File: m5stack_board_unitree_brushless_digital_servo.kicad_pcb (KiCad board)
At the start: 2 copper layers, 50 x 35 mm, 28 parts, among them J1 XT30UPB-M, J2 ZX-HY2.0-4PZZ, J3 B3B-PH-K-S(LF)(SN), J4 B3B-PH-K-S(LF)(SN), J5 B3B-PH-K-S(LF)(SN), J6 B3B-PH-K-S(LF)(SN), J7 B3B-PH-K-S(LF)(SN), U1 74LVC1G14, U2 AP7333-33SAG, U3 74LVC1G126, U4 74LVC1G125

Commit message: Use the Basic part XC6206P332MR for U2
U2 was the AP7333-33SAG carried over from the DYNAMIXEL board: an Extended
part with the lowest stock in the BOM (about 16k). The Torex XC6206P332MR-G
(C5446) is a Basic part (no feeder loading fee in Economic PCBA, about 420k
in stock) and covers the few mA the logic draws (200 mA, 6 V input, stable
with the 1 uF C2 and C3).

Its pins differ (1 GND, 2 output, 3 input), so:
- the schematic uses the KiCad XC6206PxxxMR symbol (same pin positions);
- on the board, C2 + feeds pin 3, pin 1 gets a GND via above it, the +5V
  line above U2 moves up 0.45 mm to keep that via clear of its pour
  clearance, and C2 - now joins C3 -;
- the CPL keeps +180 (same land pattern orientation as before).

DRC, ERC and the board checks are clean; the README images are updated.

Co-Authored-By: Claude Opus 5.5 <noreply@anthropic.com>
Claude-Session: https://claude.ai/code/session_01WJ1YBGdXpG8xhBv94Snq4Y
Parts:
- U2: value AP7333-33SAG -> XC6206P332MR
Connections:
- U2 pad 1: +5V -> GND
- U2 pad 3: GND -> +5V
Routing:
- net +5V: track 18.6 -> 19.6 mm
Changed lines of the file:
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@@
 			)
 		)
-		(property "Value" "AP7333-33SAG"
+		(property "Value" "XC6206P332MR"
 			(at 0 2.4 0)
 			(layer "F.Fab")
@@
 			)
 		)
-		(property "Datasheet" "https://www.diodes.com/assets/Datasheets/AP7384.pdf"
+		(property "Datasheet" "https://www.torexsemi.com/file/xc6206/XC6206.pdf"
 			(at 0 0 0)
 			(layer "F.Fab")
@@
 			)
 		)
-		(property "LCSC" "C150746"
+		(property "LCSC" "C5446"
 			(at 0 0 0)
 			(layer "F.Fab")
@@
 			(layers "F.Cu" "F.Mask" "F.Paste")
 			(roundrect_rratio 0.25)
-			(net 5 "+5V")
+			(net 2 "GND")
 		)
 		(pad "2" smd roundrect
@@
 			(layers "F.Cu" "F.Mask" "F.Paste")
 			(roundrect_rratio 0.25)
-			(net 2 "GND")
+			(net 5 "+5V")
 		)
 		(embedded_fonts no)
@@
 	)
 	(segment
+		(start 152.963 121.3)
+		(end 152.963 120.55)
+		(width 0.4)
+		(layer "F.Cu")
+		(net 2)
+	)
+	(segment
 		(start 158.3 121.3875)
 		(end 158.3 120.35)
@@
 	)
 	(segment
-		(start 156.7 123.1125)
-		(end 154.84 121.45)
+		(start 156.7 123.112)
+		(end 158.3 121.512)
 		(width 0.4)
 		(layer "F.Cu")
@@
 	)
 	(segment
-		(start 154.8375 122.25)
-		(end 154.84 121.45)
-		(width 0.4)
-		(layer "F.Cu")
-		(net 2)
-	)
-	(segment
 		(start 146 123.1)
 		(end 147.35 123.1)
@@
 	)
 	(via
-		(at 154.84 121.45)
+		(at 152.963 120.55)
 		(size 0.605)
 		(drill 0.3)
@@
 	)
 	(segment
-		(start 152.96 119.75)
-		(end 156.2 119.75)
+		(start 155.6 122.25)
+		(end 156.462 121.388)
 		(width 0.5)
 		(layer "F.Cu")
@@
 	)
 	(segment
-		(start 145.8 119.75)
-		(end 152.96 119.75)
+		(start 155.75 119.3)
+		(end 156.7 120.25)
 		(width 0.5)
 		(layer "F.Cu")
@@
 	)
 	(segment
-		(start 152.96 119.75)
-		(end 152.9625 121.3)
+		(start 151 119.75)
+		(end 151.45 119.3)
+		(width 0.5)
+		(layer "F.Cu")
+		(net 5)
+	)
+	(segment
+		(start 151.45 119.3)
+		(end 155.75 119.3)
+		(width 0.5)
+		(layer "F.Cu")
+		(net 5)
+	)
+	(segment
+		(start 156.462 121.388)
+		(end 156.7 121.388)
 		(width 0.5)
 		(layer "F.Cu")
@@
 	)
 	(segment
-		(start 156.2 119.75)
-		(end 156.7 120.25)
+		(start 145.8 119.75)
+		(end 151 119.75)
+		(width 0.5)
+		(layer "F.Cu")
+		(net 5)
+	)
+	(segment
+		(start 154.838 122.25)
+		(end 155.6 122.25)
 		(width 0.5)
 		(layer "F.Cu")

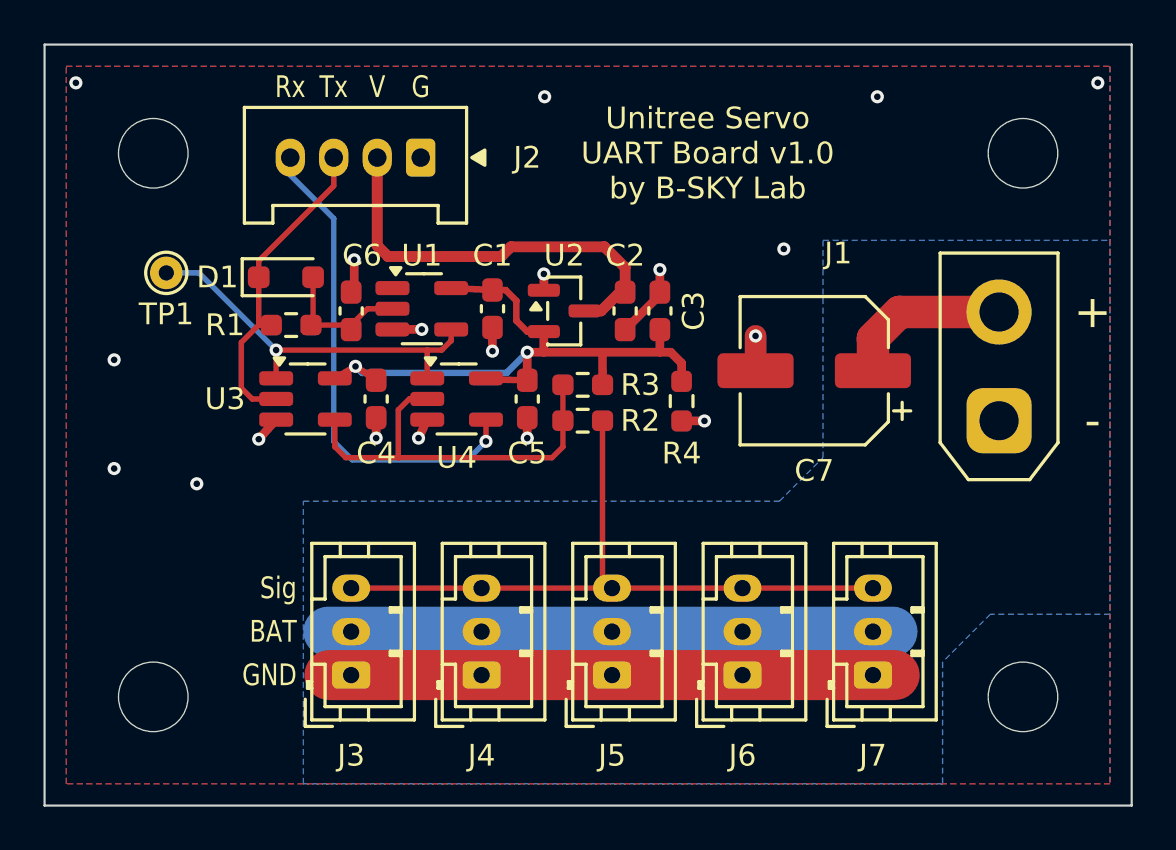
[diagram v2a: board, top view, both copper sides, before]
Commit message: Add the servo power fuse and pre-order fixes (ordered as 062722a) (#1)
* Add a MINI blade fuse F1 between J1 and BAT

BAT had no protection: a short on the board or in the servo wiring would let
the battery drive a large current with nothing to break it. F1 takes a MINI
blade fuse (ISO 8820-3, 32 V, 1000 A breaking capacity), which car parts shops
in Japan sell; the fuse itself is user supplied. 15 A covers five J288 servos
(9.6 A worst case) and stays within the XT30 rating.

- Footprint: two Keystone 3557 universal clips (LCSC C2680614, wave soldered
  in Economic PCBA) 9.73 mm apart, per the Keystone layout for MINI fuses,
  bodies facing each other; pads fully connected to the pours.
- Schematic: J1 + -> BAT_IN -> F1 -> BAT -> C7 and the ports.
- Board: F1 stands just left of J1 where C7 was. BAT_IN is an F.Cu pour from
  J1 + to the top clip; the bottom clip goes straight into the B.Cu BAT band
  under the ports. C7 moves to the top strip (body 2.57 mm from the edge) and
  reaches BAT through a via into the B.Cu BAT pour, which now also runs up the
  left of F1. The board name moves to the back silkscreen.
- JLCPCB: the export lists F1 as two clips, F1A and F1B, each at the middle
  of its tails, rotated to match the EasyEDA land pattern.
- pincheck: J1 pin 2 is BAT_IN; F1 is BAT_IN / BAT.

DRC (with schematic parity), ERC and the board checks are clean.

Co-Authored-By: Claude Opus 5.5 <noreply@anthropic.com>
Claude-Session: https://claude.ai/code/session_01WJ1YBGdXpG8xhBv94Snq4Y

* Document the fuse

README: pin assignment, how to choose the fuse rating, specifications, BOM,
the F1A / F1B clips in the JLCPCB files and the 3D model command. Design
document: the decision and its reasons, the layout, the footprint and the
JLCPCB handling, and the protection still missing (reverse polarity, ESD).
The README images show the new layout.

Co-Authored-By: Claude Opus 5.5 <noreply@anthropic.com>
Claude-Session: https://claude.ai/code/session_01WJ1YBGdXpG8xhBv94Snq4Y

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
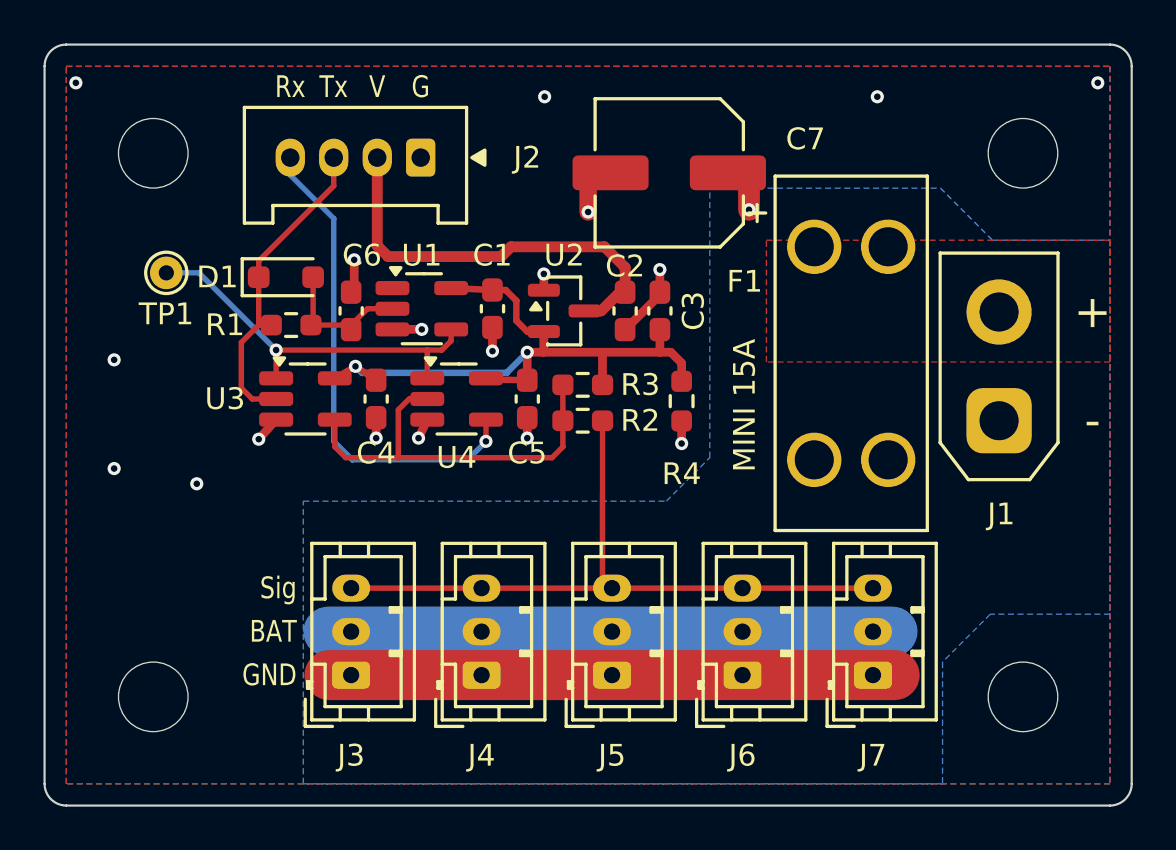
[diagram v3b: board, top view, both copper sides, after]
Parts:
- added F1: MINI 15A, Library:Fuseholder_Blade_Mini_XFCN_XF-508P-B-B, F.Cu at (167.1, 124.2)
- R4: value 2.2k -> 470
- moved C7 11.3 mm to (158.7, 115.9)
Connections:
- J1 pad 2: /BAT -> /BAT_IN
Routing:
- net /BAT: track 33.7 -> 27.8 mm, vias 0 -> 1
- net GND: track 40.6 -> 41.0 mm, vias 19 -> 18
- added copper zone on F.Cu, net /BAT_IN
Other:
- outline, holes or cut-outs redrawn
